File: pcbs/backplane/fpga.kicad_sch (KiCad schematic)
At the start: 76 parts, among them J2 Conn_02x15_Odd_Even, J3 Conn_02x20_Odd_Even, Q10 MMBT3906, Q11 MMBT3906, Q9 D44H11G, U10 74LVC2T45, U28 Snickerdoodle, U34 ICS501, U4 PCA9544APW, U5 PCA9544APW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

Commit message: Finished migrating footprint names
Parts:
- TP4, TP50, TP51, TP6, TP7, TP8, TP9: footprint TestPoint:TestPoint_Keystone_5019_Minature -> TestPoint:TestPoint_Keystone_5019_Miniature
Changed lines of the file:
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@@
 			)
 		)
-		(property "Footprint" "TestPoint:TestPoint_Keystone_5019_Minature"
+		(property "Footprint" "TestPoint:TestPoint_Keystone_5019_Miniature"
 			(at 392.43 204.47 0)
 			(effects
@@
 			)
 		)
-		(property "Footprint" "TestPoint:TestPoint_Keystone_5019_Minature"
+		(property "Footprint" "TestPoint:TestPoint_Keystone_5019_Miniature"
 			(at 392.43 101.6 0)
 			(effects
@@
 			)
 		)
-		(property "Footprint" "TestPoint:TestPoint_Keystone_5019_Minature"
+		(property "Footprint" "TestPoint:TestPoint_Keystone_5019_Miniature"
 			(at 407.67 219.71 0)
 			(effects
@@
 			)
 		)
-		(property "Footprint" "TestPoint:TestPoint_Keystone_5019_Minature"
+		(property "Footprint" "TestPoint:TestPoint_Keystone_5019_Miniature"
 			(at 407.67 229.87 0)
 			(effects
@@
 			)
 		)
-		(property "Footprint" "TestPoint:TestPoint_Keystone_5019_Minature"
+		(property "Footprint" "TestPoint:TestPoint_Keystone_5019_Miniature"
 			(at 407.67 224.79 0)
 			(effects
@@
 			)
 		)
-		(property "Footprint" "TestPoint:TestPoint_Keystone_5019_Minature"
+		(property "Footprint" "TestPoint:TestPoint_Keystone_5019_Miniature"
 			(at 407.67 204.47 0)
 			(effects
@@
 			)
 		)
-		(property "Footprint" "TestPoint:TestPoint_Keystone_5019_Minature"
+		(property "Footprint" "TestPoint:TestPoint_Keystone_5019_Miniature"
 			(at 407.67 194.31 0)
 			(effects

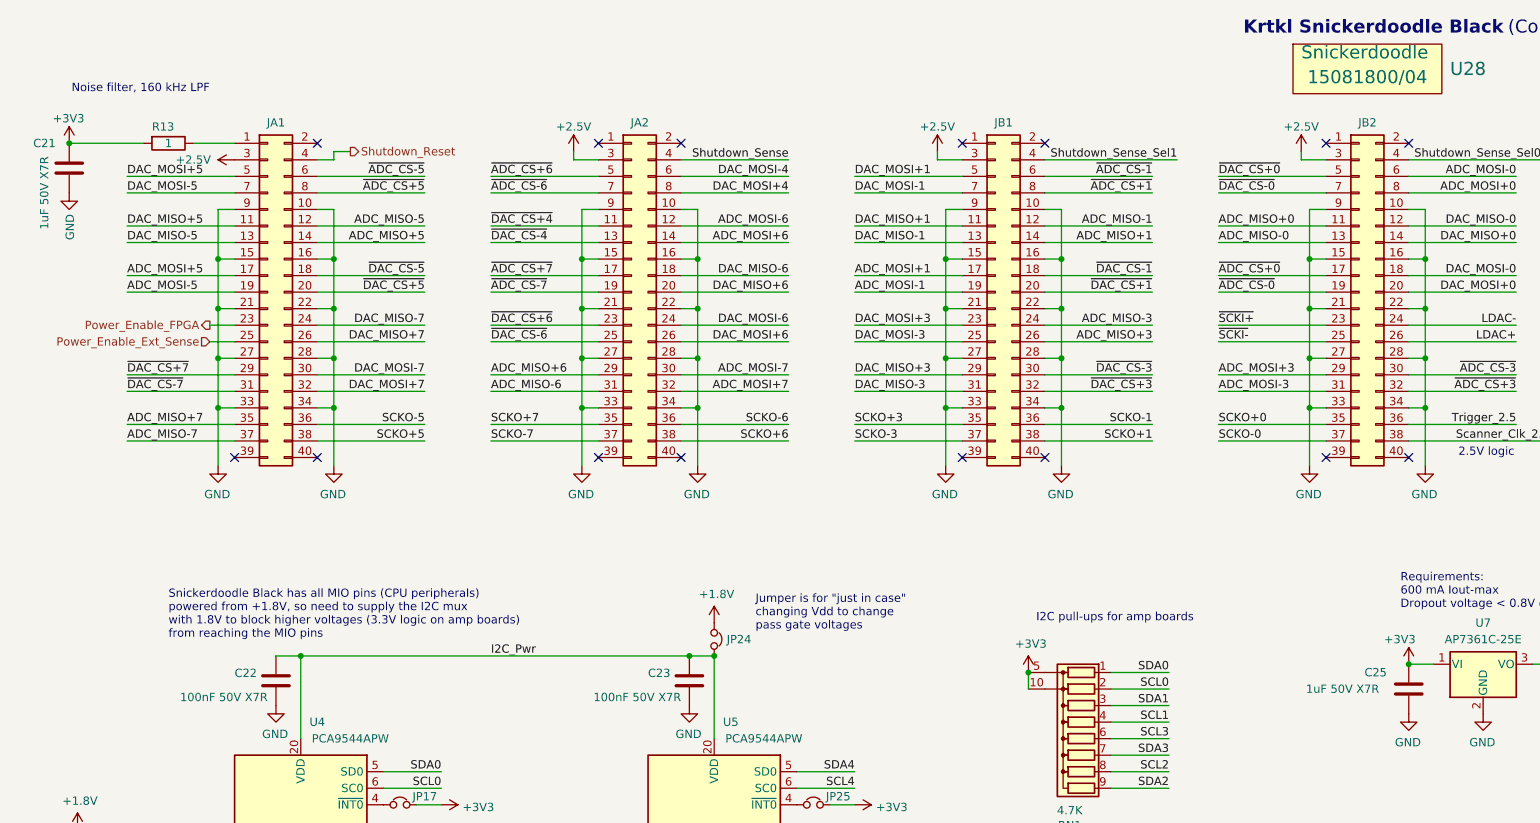
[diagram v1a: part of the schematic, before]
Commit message: Functional fixes for ADC clk, +3.3V sag on backplane
Amp ctrl: Added ADC clock inversion (fixes #34)
Backplane: fixed series-resistor-induced voltage sag (fixes #33)
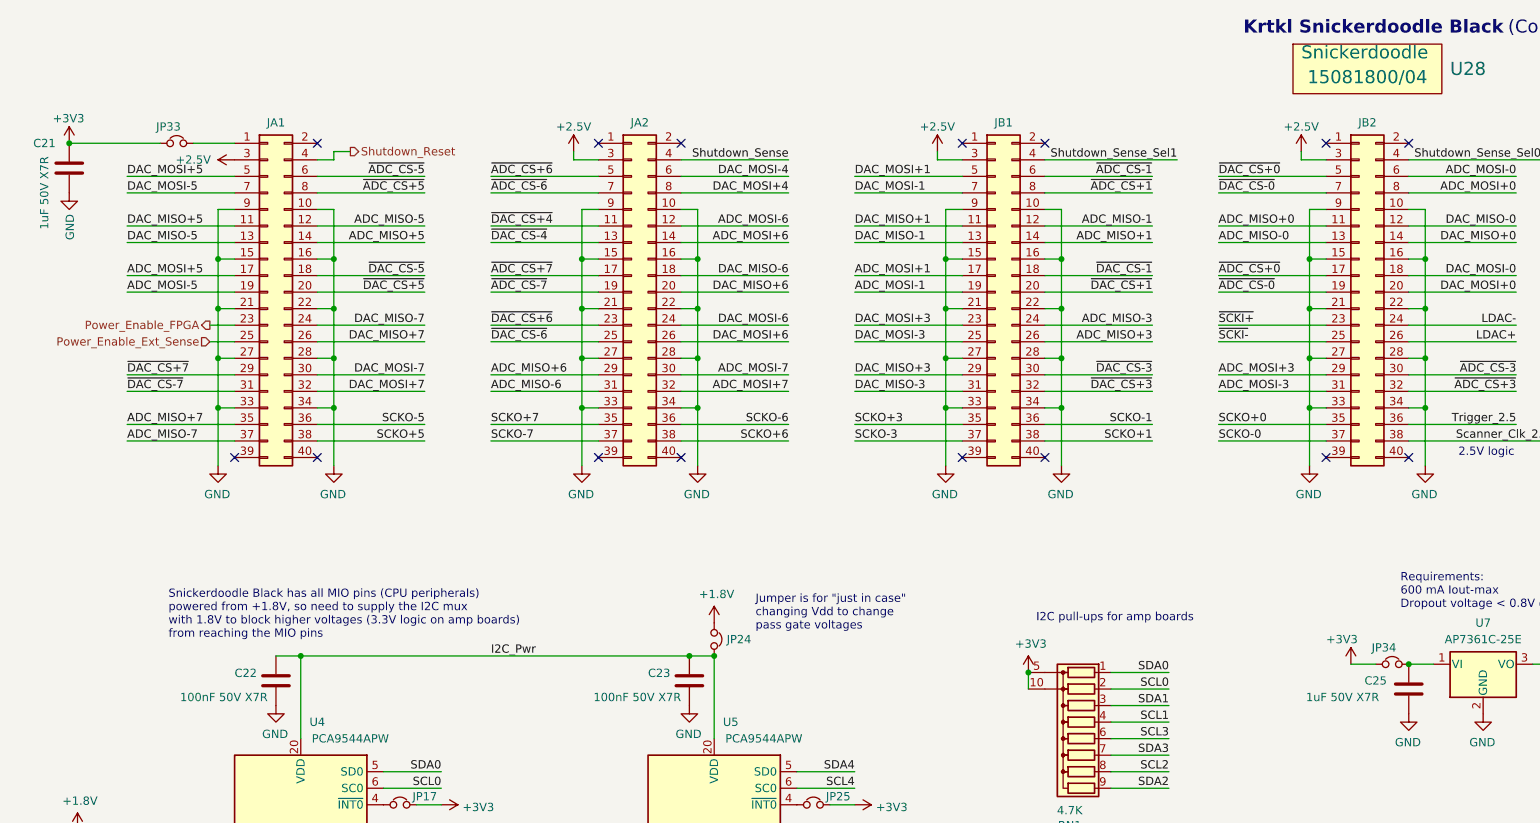
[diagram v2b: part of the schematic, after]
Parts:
- removed R13: 1, Resistor_SMD:R_0805_2012Metric, symbol Device:R
- added JP33, JP34: Jumper_NC_Small, Jumper:SolderJumper-2_P1.3mm_Bridged_RoundedPad1.0x1.5mm, symbol backplane-rescue:Jumper_NC_Small-Device
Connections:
- net +3V3: now also JP33.1, JP34.1; no longer C25.2, U7.1 (VI)
- net at JA1.1 (Pin_1): now also JP33.2
- new net: C25.2, JP34.2, U7.1 (VI)
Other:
- note removed: "Noise filter, 160 kHz LPF"
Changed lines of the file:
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@@
 		(comment 1 "Don Straney")
 	)
-	(text "Noise filter, 160 kHz LPF"
-		(exclude_from_sim no)
-		(at 44.45 25.4 0)
-		(effects
-			(font
-				(size 1.27 1.27)
-			)
-			(justify right bottom)
-		)
-	)
 	(text "Requirements:\n600 mA Iout-max\nDropout voltage < 0.8V @ 600 mA"
 		(exclude_from_sim no)
@@
 	(wire
 		(pts
-			(xy 22.86 33.02) (xy 34.29 33.02)
+			(xy 22.86 33.02) (xy 36.83 33.02)
 		)
 		(stroke
@@
 		)
 	)
+	(wire
+		(pts
+			(xy 219.71 113.03) (xy 223.52 113.03)
+		)
+		(stroke
+			(width 0)
+			(type default)
+		)
+	)
 	(bus
 		(pts
@@
 		(dnp no)
 		(property "Reference" "C25"
-			(at 223.52 114.3 0)
+			(at 223.52 115.57 0)
 			(effects
 				(font
@@
 		)
 		(property "Value" "1uF 50V X7R"
-			(at 218.44 116.84 0)
+			(at 218.44 118.11 0)
 			(effects
 				(font
@@
 	(symbol
 		(lib_id "backplane-rescue:+3.3V-power")
-		(at 228.6 113.03 0)
+		(at 219.71 113.03 0)
 		(unit 1)
 		(exclude_from_sim no)
@@
 		(dnp no)
 		(property "Reference" "#PWR0244"
-			(at 228.6 116.84 0)
+			(at 219.71 116.84 0)
 			(effects
 				(font
@@
 		)
 		(property "Value" "+3V3"
-			(at 224.79 109.22 0)
+			(at 215.9 109.22 0)
 			(effects
 				(font
@@
 		)
 		(property "Footprint" ""
-			(at 228.6 113.03 0)
+			(at 219.71 113.03 0)
 			(effects
 				(font
@@
 		)
 		(property "Datasheet" ""
-			(at 228.6 113.03 0)
+			(at 219.71 113.03 0)
 			(effects
 				(font
@@
 		)
 		(property "Description" ""
-			(at 228.6 113.03 0)
+			(at 219.71 113.03 0)
 			(effects
 				(font
@@
 	)
 	(symbol
-		(lib_id "Device:R")
-		(at 38.1 33.02 270)
-		(unit 1)
-		(exclude_from_sim no)
-		(in_bom yes)
-		(on_board yes)
-		(dnp no)
-		(property "Reference" "R13"
-			(at 35.56 30.48 90)
-			(effects
-				(font
-					(size 1.27 1.27)
-				)
-				(justify left)
-			)
-		)
-		(property "Value" "1"
-			(at 38.1 33.02 90)
-			(effects
-				(font
-					(size 1.27 1.27)
-				)
-			)
-		)
-		(property "Footprint" "Resistor_SMD:R_0805_2012Metric"
-			(at 38.1 31.242 90)
-			(effects
-				(font
-					(size 1.27 1.27)
-				)
-				(hide yes)
-			)
-		)
-		(property "Datasheet" "~"
-			(at 38.1 33.02 0)
-			(effects
-				(font
-					(size 1.27 1.27)
-				)
-				(hide yes)
-			)
-		)
-		(property "Description" ""
-			(at 38.1 33.02 0)
-			(effects
-				(font
-					(size 1.27 1.27)
-				)
-				(hide yes)
-			)
-		)
-		(property "Manufacturer" "KOA Speer"
-			(at 38.1 33.02 0)
-			(effects
-				(font
-					(size 1.27 1.27)
-				)
-				(hide yes)
-			)
-		)
-		(property "Notes" "Can substitute generic resistor with same package, value, 1% tolerance"
-			(at 38.1 33.02 0)
-			(effects
-				(font
-					(size 1.27 1.27)
-				)
-				(hide yes)
-			)
-		)
-		(property "Part Number" "RK73H2ATTD1R00F"
-			(at 38.1 33.02 0)
-			(effects
-				(font
-					(size 1.27 1.27)
-				)
-				(hide yes)
-			)
-		)
-		(property "Type" "SMT"
-			(at 38.1 33.02 0)
-			(effects
-				(font
-					(size 1.27 1.27)
-				)
-				(hide yes)
-			)
-		)
-		(pin "1"
-		)
-		(pin "2"
-		)
-		(instances
-			(project "backplane"
-				(path "/4cff6540-dfbc-472e-b6ee-b480e176be3d/00000000-0000-0000-0000-000060af9c81"
-					(reference "R13")
-					(unit 1)
-				)
-			)
-		)
-	)
-	(symbol
 		(lib_id "Device:C")
 		(at 22.86 36.83 180)
@@
 	)
 	(symbol
+		(lib_id "backplane-rescue:Jumper_NC_Small-Device")
+		(at 39.37 33.02 0)
+		(unit 1)
+		(exclude_from_sim no)
+		(in_bom no)
+		(on_board yes)
+		(dnp no)
+		(property "Reference" "JP33"
+			(at 38.1 30.48 0)
+			(effects
+				(font
+					(size 1.27 1.27)
+				)
+			)
+		)
+		(property "Value" "Jumper_NC_Small"
+			(at 39.37 29.9466 0)
+			(effects
+				(font
+					(size 1.27 1.27)
+				)
+				(hide yes)
+			)
+		)
+		(property "Footprint" "Jumper:SolderJumper-2_P1.3mm_Bridged_RoundedPad1.0x1.5mm"
+			(at 39.37 33.02 0)
+			(effects
+				(font
+					(size 1.27 1.27)
+				)
+				(hide yes)
+			)
+		)
+		(property "Datasheet" "~"
+			(at 39.37 33.02 0)
+			(effects
+				(font
+					(size 1.27 1.27)
+				)
+				(hide yes)
+			)
+		)
+		(property "Description" ""
+			(at 39.37 33.02 0)
+			(effects
+				(font
+					(size 1.27 1.27)
+				)
+				(hide yes)
+			)
+		)
+		(pin "1"
+		)
+		(pin "2"
+		)
+		(instances
+			(project "backplane"
+				(path "/4cff6540-dfbc-472e-b6ee-b480e176be3d/00000000-0000-0000-0000-000060af9c81"
+					(reference "JP33")
+					(unit 1)
+				)
+			)
+		)
+	)
+	(symbol
 		(lib_id "Device:R")
 		(at 364.49 115.57 180)
@@
 					(unit 1)
 				)
+			)
+		)
+	)
+	(symbol
+		(lib_id "backplane-rescue:Jumper_NC_Small-Device")
+		(at 226.06 113.03 0)
+		(unit 1)
+		(exclude_from_sim no)
+		(in_bom no)
+		(on_board yes)
+		(dnp no)
+		(property "Reference" "JP34"
+			(at 224.79 110.49 0)
+			(effects
+				(font
+					(size 1.27 1.27)
+				)
+			)
+		)
+		(property "Value" "Jumper_NC_Small"
+			(at 226.06 109.9566 0)
+			(effects
+				(font
+					(size 1.27 1.27)
+				)
+				(hide yes)
+			)
+		)
+		(property "Footprint" "Jumper:SolderJumper-2_P1.3mm_Bridged_RoundedPad1.0x1.5mm"
+			(at 226.06 113.03 0)
+			(effects
+				(font
+					(size 1.27 1.27)
+				)
+				(hide yes)
+			)
+		)
+		(property "Datasheet" "~"
+			(at 226.06 113.03 0)
+			(effects
+				(font
+					(size 1.27 1.27)
+				)
+				(hide yes)
+			)
+		)
+		(property "Description" ""
+			(at 226.06 113.03 0)
+			(effects
+				(font
+					(size 1.27 1.27)
+				)
+				(hide yes)
+			)
+		)
+		(pin "1"
+		)
+		(pin "2"
+		)
+		(instances
+			(project "backplane"
+				(path "/4cff6540-dfbc-472e-b6ee-b480e176be3d/00000000-0000-0000-0000-000060af9c81"
+					(reference "JP34")
+					(unit 1)
+				)

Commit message: BOM & reset fixes
Amp ctrl: changed name of "Manufacturer" field to "MPN" to work with Aisler
Amp ctrl: added part number to logic inverter, corrected various typos and part number problems
Backplane: added pull-down to Shutdown_Reset signal (#35)
Backplane: rethought Shutdown_Force circuit to make fail-safe (broken connections->shutdown), make work correctly (fixes #35)
Backplane: updated/corrected various schematic annotations
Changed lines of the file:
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@@
 	)
 	(junction
+		(at 381 101.6)
+		(diameter 0)
+		(color 0 0 0 0)
+	)
+	(junction
 		(at 33.02 152.4)
 		(diameter 0)
@@
 	(wire
 		(pts
-			(xy 368.3 101.6) (xy 387.35 101.6)
+			(xy 368.3 101.6) (xy 381 101.6)
 		)
 		(stroke
@@
 	(wire
 		(pts
+			(xy 381 101.6) (xy 387.35 101.6)
+		)
+		(stroke
+			(width 0)
+			(type default)
+		)
+	)
+	(wire
+		(pts
 			(xy 340.36 73.66) (xy 342.9 73.66)
 		)
@@
 		)
 	)
-	(label "FPGA_Vin"
-		(at 377.19 101.6 180)
-		(effects
-			(font
-				(size 1.27 1.27)
-			)
-			(justify right bottom)
-		)
-	)
 	(label "SDA2"
 		(at 80.01 149.86 180)
@@
 					(unit 1)
 				)
+			)
+		)
+	)
+	(symbol
+		(lib_name "VD_1")
+		(lib_id "power:VD")
+		(at 381 101.6 0)
+		(unit 1)
+		(exclude_from_sim no)
+		(in_bom yes)
+		(on_board yes)
+		(dnp no)
+		(property "Reference" "#PWR024"
+			(at 381 105.41 0)
+			(effects
+				(font
+					(size 1.27 1.27)
+				)
+				(hide yes)
+			)
+		)
+		(property "Value" "FPGA_Vin"
+			(at 381 97.79 0)
+			(effects
+				(font
+					(size 1.27 1.27)
+				)
+			)
+		)
+		(property "Footprint" ""
+			(at 381 101.6 0)
+			(effects
+				(font
+					(size 1.27 1.27)
+				)
+				(hide yes)
+			)
+		)
+		(property "Datasheet" ""
+			(at 381 101.6 0)
+			(effects
+				(font
+					(size 1.27 1.27)
+				)
+				(hide yes)
+			)
+		)
+		(property "Description" "Power symbol creates a global label with name \"VD\""
+			(at 381 101.6 0)
+			(effects
+				(font
+					(size 1.27 1.27)
+				)
+				(hide yes)
+			)
+		)
+		(pin "1"
+		)
+		(instances
+			(project ""
+				(path "/4cff6540-dfbc-472e-b6ee-b480e176be3d/00000000-0000-0000-0000-000060af9c81"
+					(reference "#PWR024")
+					(unit 1)
+				)
